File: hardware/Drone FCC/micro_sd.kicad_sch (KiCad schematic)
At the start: 20 parts, among them J701 DM3AT-SF-PEJM5

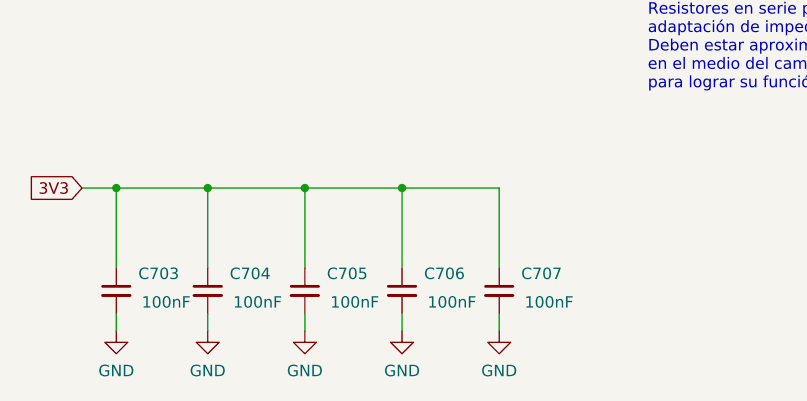
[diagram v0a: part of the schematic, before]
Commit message: rounded corners
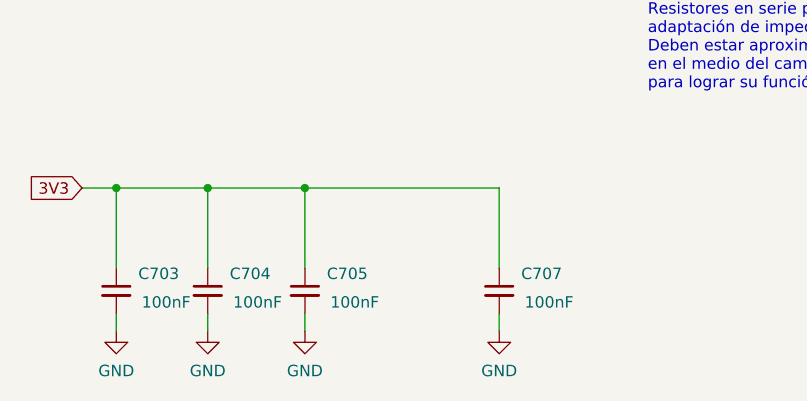
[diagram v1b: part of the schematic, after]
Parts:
- removed C706: 100nF, Capacitor_SMD:C_0402_1005Metric_Pad0.74x0.62mm_HandSolder, symbol Device:C_Small
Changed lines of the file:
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@@
 (kicad_sch (version 20211123) (generator eeschema)
   (paper "A4")
-  (junction (at 73.025 150.495) (diameter 0) (color 0 0 0 0)
-  )
   (junction (at 41.275 150.495) (diameter 0) (color 0 0 0 0)
   )
@@
     (stroke (width 0) (type default) (color 0 0 0 0))
   )
-  (wire (pts (xy 73.025 164.465) (xy 73.025 166.37))
-    (stroke (width 0) (type default) (color 0 0 0 0))
-  )
   (wire (pts (xy 165.1 72.39) (xy 176.53 72.39))
     (stroke (width 0) (type default) (color 0 0 0 0))
@@
     (stroke (width 0) (type default) (color 0 0 0 0))
   )
-  (wire (pts (xy 62.23 150.495) (xy 73.025 150.495))
-    (stroke (width 0) (type default) (color 0 0 0 0))
-  )
   (polyline (pts (xy 173.99 69.85) (xy 195.58 69.85))
     (stroke (width 0) (type default) (color 0 0 0 0))
@@
     (stroke (width 0) (type default) (color 0 0 0 0))
   )
-  (wire (pts (xy 73.025 159.385) (xy 73.025 150.495))
-    (stroke (width 0) (type default) (color 0 0 0 0))
-  )
   (wire (pts (xy 115.57 74.93) (xy 115.57 72.39))
     (stroke (width 0) (type default) (color 0 0 0 0))
@@
     (stroke (width 0) (type default) (color 0 0 0 0))
   )
-  (wire (pts (xy 73.025 150.495) (xy 83.82 150.495))
+  (wire (pts (xy 62.23 150.495) (xy 83.82 150.495))
     (stroke (width 0) (type default) (color 0 0 0 0))
   )
@@
     )
     (property "Datasheet" "~" (id 3) (at 83.82 161.925 0)
-      (effects (font (size 1.27 1.27)) hide)
-    )
-    (pin "1")
-    (pin "2")
-  )
-  (symbol (lib_id "Device:C_Small") (at 73.025 161.925 0) (unit 1)
-    (in_bom yes) (on_board yes)
-    (property "Reference" "C706" (id 0) (at 80.01 160.02 0)
-      (effects (font (size 1.27 1.27)) (justify right))
-    )
-    (property "Value" "100nF" (id 1) (at 81.28 163.195 0)
-      (effects (font (size 1.27 1.27)) (justify right))
-    )
-    (property "Footprint" "Capacitor_SMD:C_0402_1005Metric_Pad0.74x0.62mm_HandSolder" (id 2) (at 73.025 161.925 0)
-      (effects (font (size 1.27 1.27)) hide)
-    )
-    (property "Datasheet" "~" (id 3) (at 73.025 161.925 0)
       (effects (font (size 1.27 1.27)) hide)
     )
@@
     (pin "2")
   )
-  (symbol (lib_id "power:GND") (at 73.025 166.37 0) (unit 1)
-    (in_bom yes) (on_board yes) (fields_autoplaced)
-    (property "Reference" "#PWR0145" (id 0) (at 73.025 172.72 0)
-      (effects (font (size 1.27 1.27)) hide)
-    )
-    (property "Value" "GND" (id 1) (at 73.025 170.815 0))
-    (property "Footprint" "" (id 2) (at 73.025 166.37 0)
-      (effects (font (size 1.27 1.27)) hide)
-    )
-    (property "Datasheet" "" (id 3) (at 73.025 166.37 0)
-      (effects (font (size 1.27 1.27)) hide)
-    )
-    (pin "1")
-  )
   (symbol (lib_id "Device:R") (at 150.495 111.125 270) (mirror x) (unit 1)

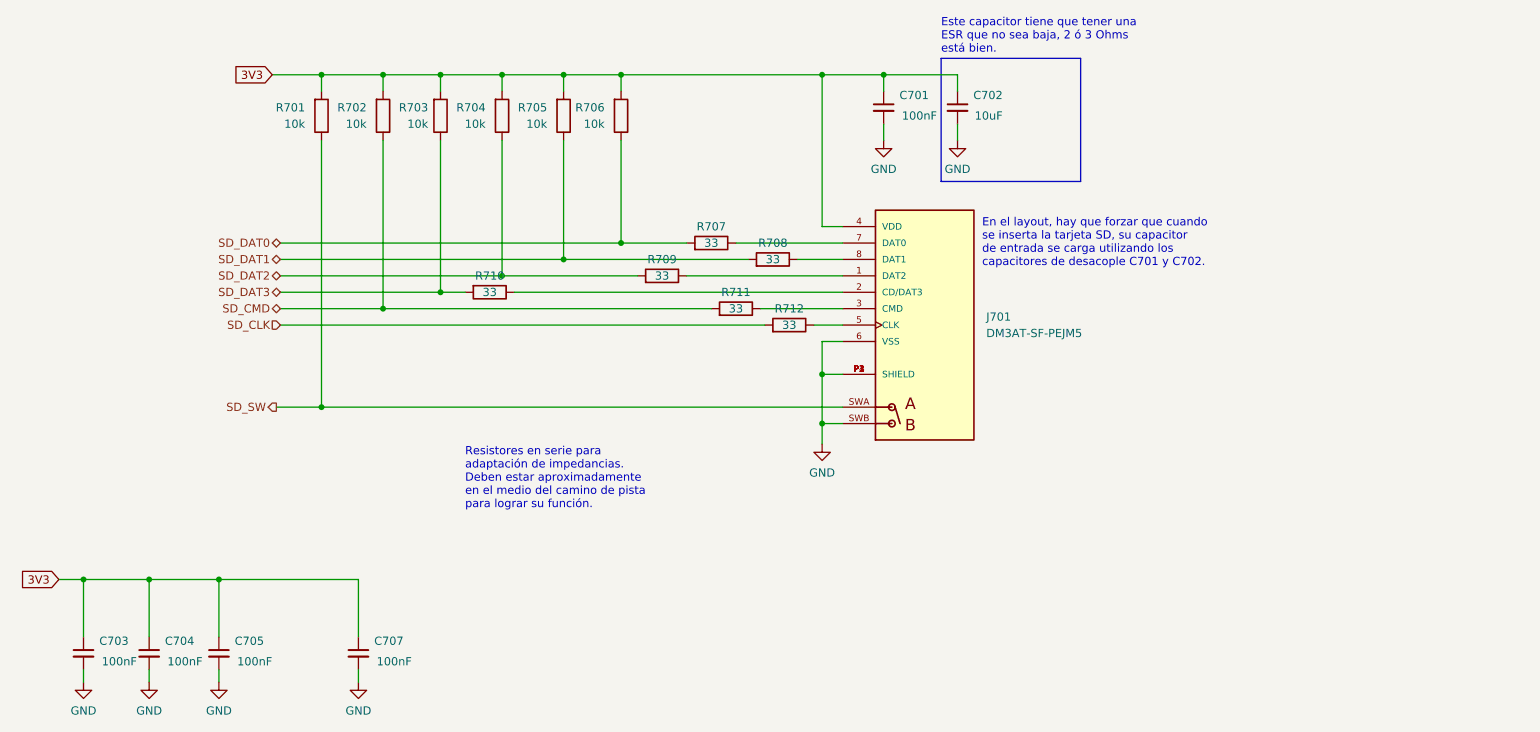
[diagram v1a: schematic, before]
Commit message: moved microSD to top layer. Also transistors for LEDs
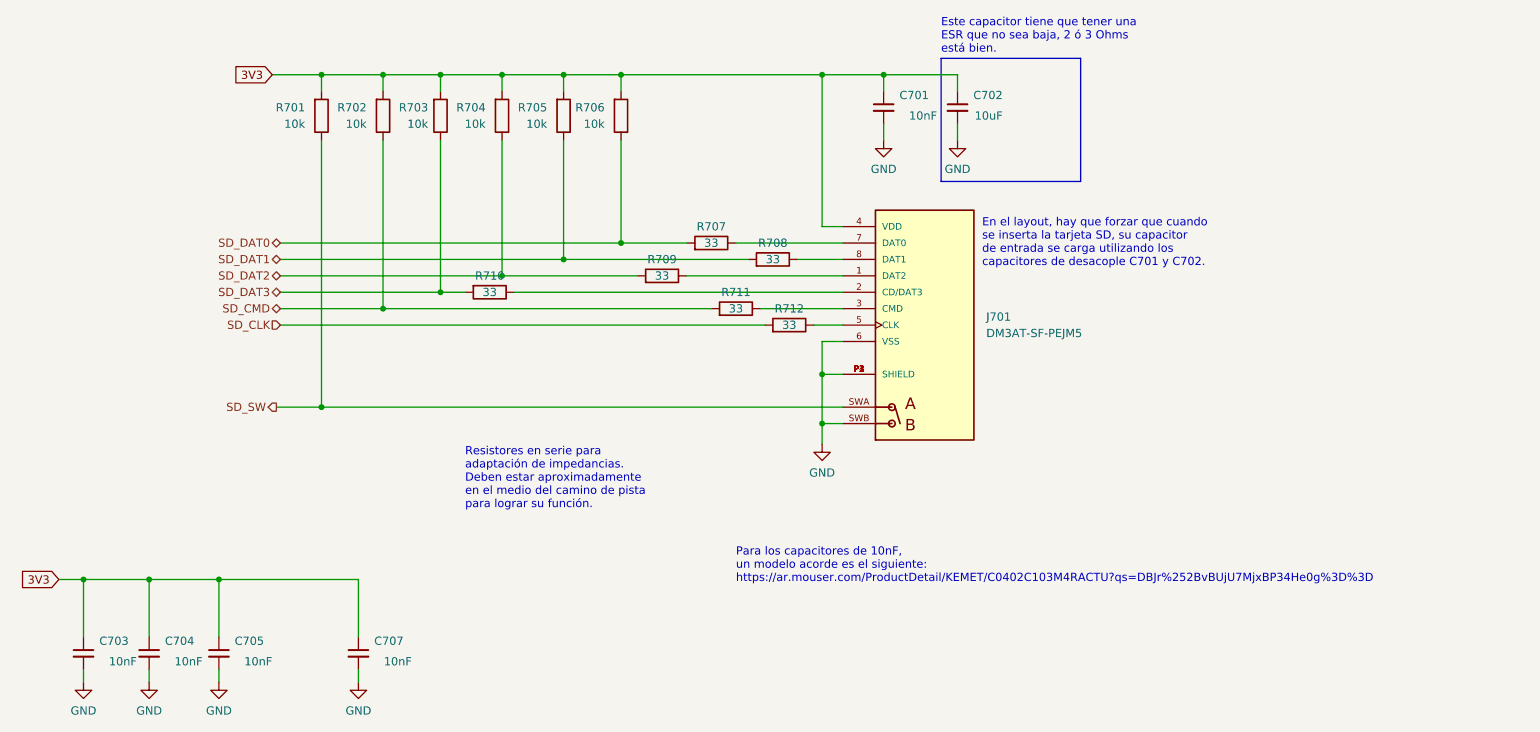
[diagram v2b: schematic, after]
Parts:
- C701, C703, C704, C705, C707: value 100nF -> 10nF
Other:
- note added: "Para los capacitores de 10nF, un modelo acorde es el siguiente: https://ar.mouser.com/ProductDetail/KEMET/C0402C103M4RACTU?qs=DBJr%252BvBUjU7MjxBP34He0g%3D%3D"
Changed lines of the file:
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@@
+    (effects (font (size 1.27 1.27)) (justify left bottom))
+  )
+  (text "Para los capacitores de 10nF,\nun modelo acorde es el siguiente:\nhttps://ar.mouser.com/ProductDetail/KEMET/C0402C103M4RACTU?qs=DBJr%252BvBUjU7MjxBP34He0g%3D%3D"
+    (at 142.24 151.13 0)
     (effects (font (size 1.27 1.27)) (justify left bottom))
   )
@@
       (effects (font (size 1.27 1.27)) (justify right))
     )
-    (property "Value" "100nF" (id 1) (at 92.075 163.195 0)
+    (property "Value" "10nF" (id 1) (at 92.075 163.195 0)
       (effects (font (size 1.27 1.27)) (justify right))
     )
@@
       (effects (font (size 1.27 1.27)) (justify right))
     )
-    (property "Value" "100nF" (id 1) (at 59.69 163.195 0)
+    (property "Value" "10nF" (id 1) (at 59.69 163.195 0)
       (effects (font (size 1.27 1.27)) (justify right))
     )
@@
       (effects (font (size 1.27 1.27)) (justify right))
     )
-    (property "Value" "100nF" (id 1) (at 173.355 78.74 0)
+    (property "Value" "10nF" (id 1) (at 173.355 78.74 0)
       (effects (font (size 1.27 1.27)) (justify right))
     )
@@
       (effects (font (size 1.27 1.27)) (justify right))
     )
-    (property "Value" "100nF" (id 1) (at 49.53 163.195 0)
+    (property "Value" "10nF" (id 1) (at 49.53 163.195 0)
       (effects (font (size 1.27 1.27)) (justify right))
     )
@@
       (effects (font (size 1.27 1.27)) (justify right))
     )
-    (property "Value" "100nF" (id 1) (at 70.485 163.195 0)
-      (effects (font (size 1.27 1.27)) (justify right))
-    )
+    (property "Value" "10nF" (id 1) (at 70.485 163.195 0)
+      (effects (font (size 1.27 1.27)) (justify right))
+    )

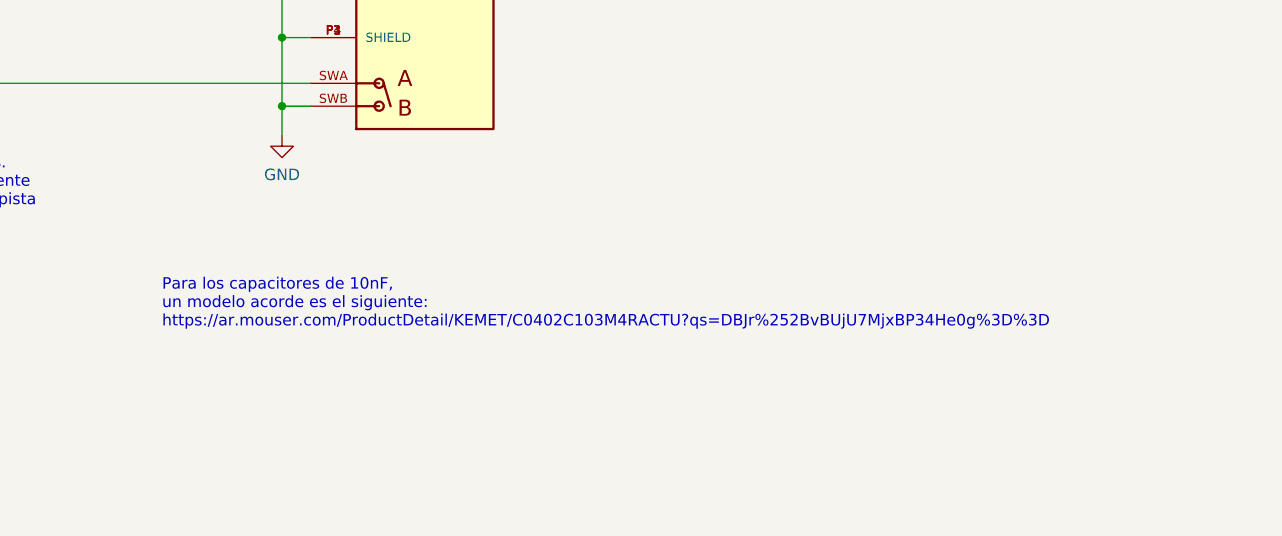
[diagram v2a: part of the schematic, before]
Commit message: length matching microSD
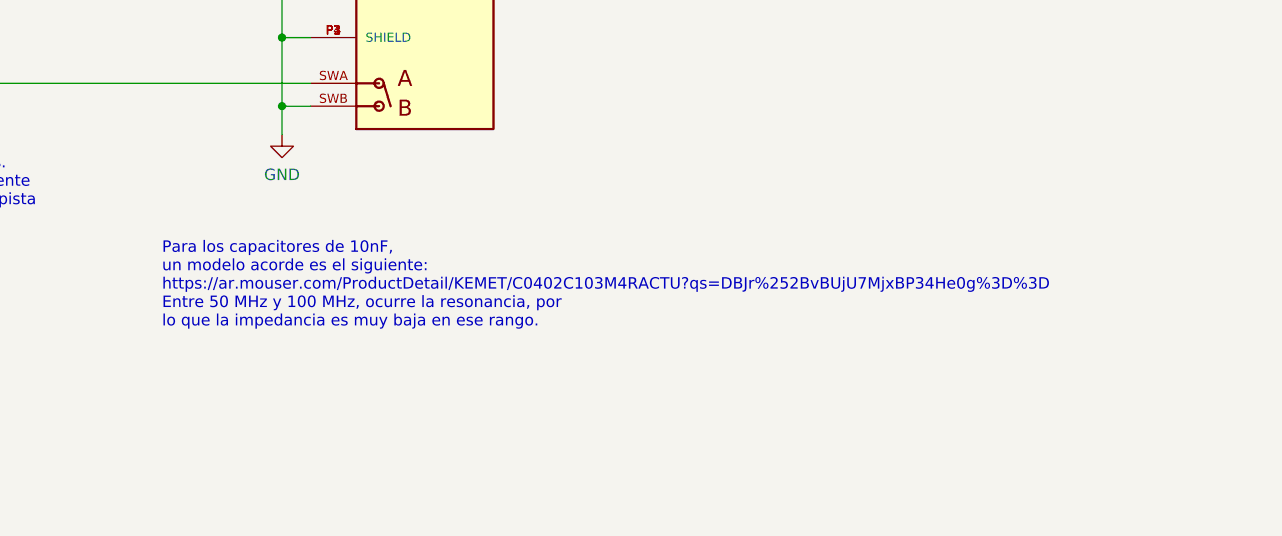
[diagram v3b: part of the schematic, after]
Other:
- note added: "Para los capacitores de 10nF, un modelo acorde es el siguiente: https://ar.mouser.com/ProductDetail/KEMET/C0402C103M4RACTU?qs=DBJr%252BvBUjU7MjxBP34He0g%3D%3D Entre 50 MHz y 100 MHz, ocurre la resonancia, por lo que la impedancia es muy baja en ese rango."
- note removed: "Para los capacitores de 10nF, un modelo acorde es el siguiente: https://ar.mouser.com/ProductDetail/KEMET/C0402C103M4RACTU?qs=DBJr%252BvBUjU7MjxBP34He0g%3D%3D"
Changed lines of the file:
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@@
     (effects (font (size 1.27 1.27)) (justify left bottom))
   )
-  (text "Para los capacitores de 10nF,\nun modelo acorde es el siguiente:\nhttps://ar.mouser.com/ProductDetail/KEMET/C0402C103M4RACTU?qs=DBJr%252BvBUjU7MjxBP34He0g%3D%3D"
+  (text "Para los capacitores de 10nF,\nun modelo acorde es el siguiente:\nhttps://ar.mouser.com/ProductDetail/KEMET/C0402C103M4RACTU?qs=DBJr%252BvBUjU7MjxBP34He0g%3D%3D\nEntre 50 MHz y 100 MHz, ocurre la resonancia, por\nlo que la impedancia es muy baja en ese rango."
     (at 142.24 151.13 0)
     (effects (font (size 1.27 1.27)) (justify left bottom))

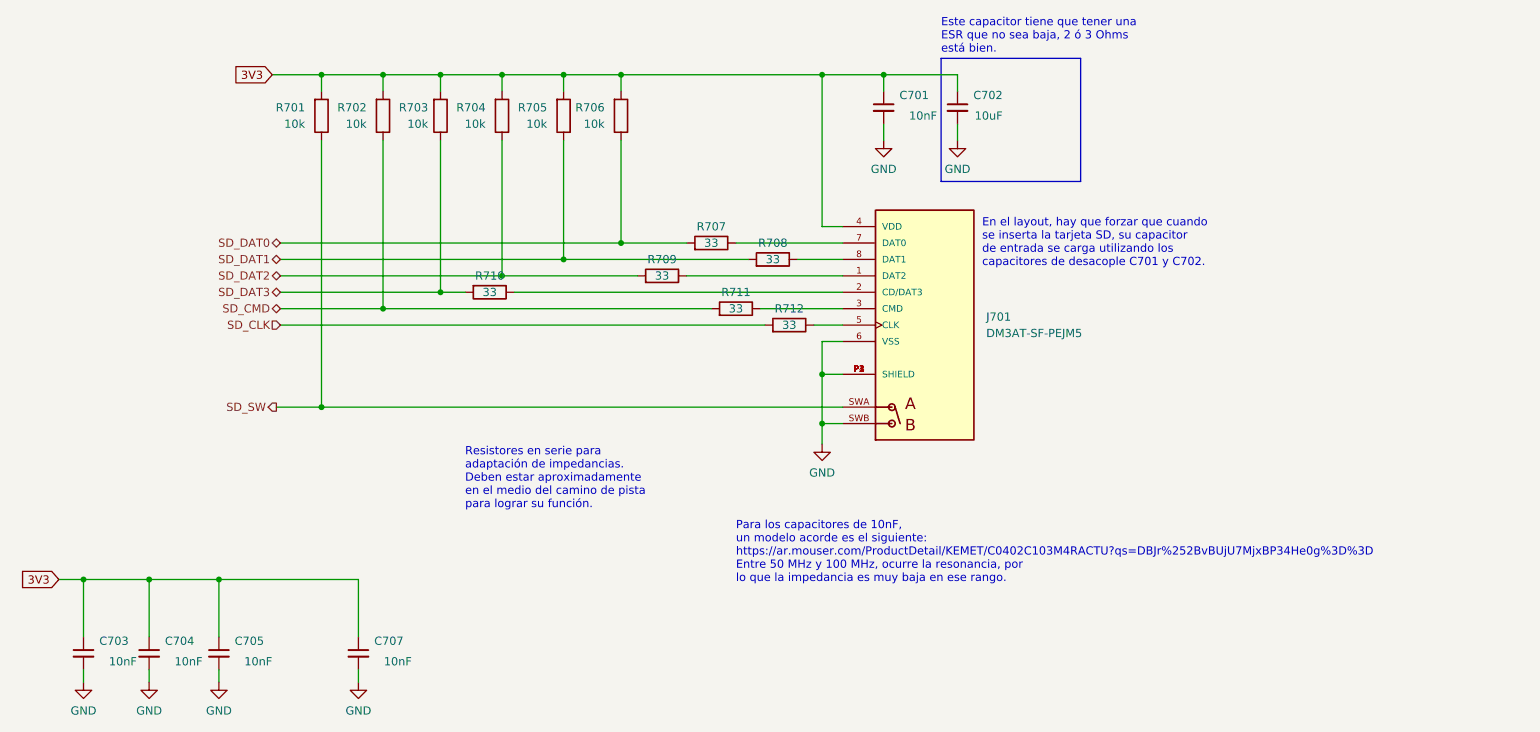
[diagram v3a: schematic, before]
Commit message: tidying up the schematic
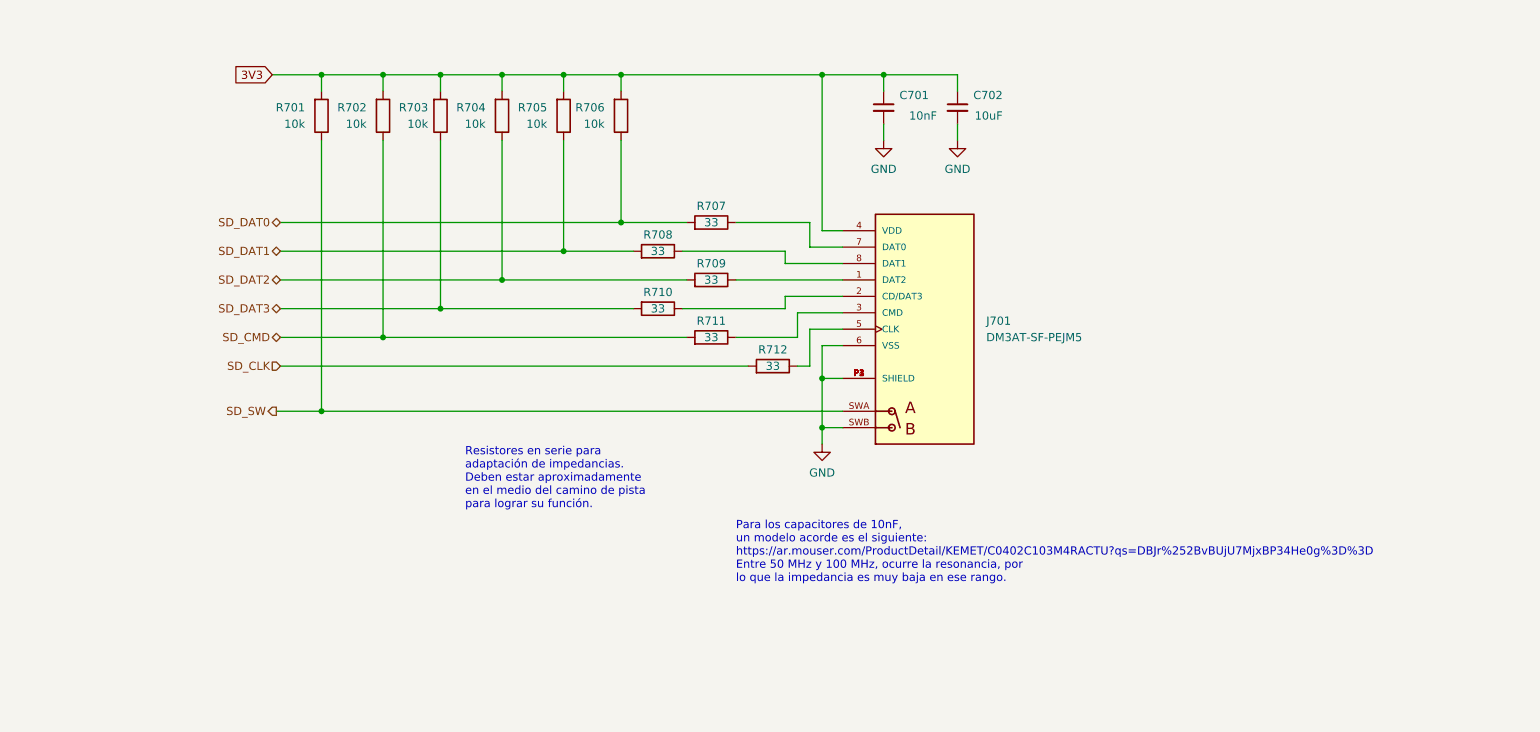
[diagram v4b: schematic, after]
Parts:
- removed C703, C704, C705, C707: 10nF, Capacitor_SMD:C_0402_1005Metric_Pad0.74x0.62mm_HandSolder, symbol Device:C_Small
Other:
- note removed: "En el layout, hay que forzar que cuando se inserta la tarjeta SD, su capacitor de entrada se carga utilizando los capacitores de desacople C701 y C702."
- note removed: "Este capacitor tiene que tener una ESR que no sea baja, 2 ó 3 Ohms está bien."
- moved on the sheet: J701, R707, R708, R709, R710, R711, R712
